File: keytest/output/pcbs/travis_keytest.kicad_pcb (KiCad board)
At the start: 2 copper layers, 51.4 x 51.4 mm, 4 parts

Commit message: key progress
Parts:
- LED1: value (none) -> SK6812mini-e
- S1: value (none) -> mx
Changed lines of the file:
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@@
   (page A3)
   (title_block
-    (title travis_key)
-    (rev 2024.03.20)
+    (title travis_keytest)
+    (rev 2024.03.21)
     (company "Travis Hardiman")
   )
@@
 (module MX (layer F.Cu)
     (at 100 100 45)
-    (fp_text reference "S1" (at 0 0) (layer F.SilkS)  (effects (font (size 1.27 1.27) (thickness 0.15))))
-    (fp_text value "" (at 0 0) (layer F.SilkS) hide (effects (font (size 1.27 1.27) (thickness 0.15))))
+    (fp_text reference "S1" (at 0 -3.25) (layer F.SilkS)  (effects (font (size 0.8 0.8) (thickness 0.15))))
+    (fp_text value "mx" (at 0 0) (layer F.SilkS) hide (effects (font (size 1 1) (thickness 0.15))))
     (fp_line (start -7 -6) (end -7 -7) (layer Dwgs.User) (width 0.15))
     (fp_line (start -7 7) (end -6 7) (layer Dwgs.User) (width 0.15))
@@
   (tags "Diode DO-35_SOD27 series Axial Horizontal pin pitch 7.62mm  length 4mm diameter 2mm")
   (at 100.0000 87.9438 315)
-  (fp_text reference "D1" (at 3.81 -2.12 315) (layer "B.SilkS")
+  (fp_text user "D1" (at 4 0 0) (layer "F.SilkS")
+    (effects (font (size 0.8 0.8) (thickness 0.15)))
+  )
+  (fp_text reference "D1" (at 5.985 1.921 315) (layer "B.SilkS")
     (effects (font (size 1 1) (thickness 0.15)) (justify mirror))
   )
-  (fp_text value "1N4148" (at 3.81 0 315) (layer "B.Fab")
-    (effects (font (size 0.8 1) (thickness 0.15)))
-  )
-  (fp_text user "K" (at 0 -1.8 315) (layer "B.SilkS")
-    (effects (font (size 1 1) (thickness 0.15)) (justify mirror))
-  )
-  (fp_text user "K" (at 0 -1.8 315) (layer "B.Fab")
-    (effects (font (size 1 1) (thickness 0.15)) (justify mirror))
+  (fp_text value "1N4148" (at 11.065 0 315) (layer "B.Fab")
+    (effects (font (size 0.8 0.8) (thickness 0.15)))
   )
   (fp_line (start 1.04 0) (end 1.69 0)
@@
   (at 103.5072 103.5072 45)
   (fp_text reference "LED1" (at -4.75 0 135) (layer B.SilkS)
-    (effects (font (size 1 1) (thickness 0.15)))
+    (effects (font (size 1 1) (thickness 0.15)) (justify mirror))
+  )
+  (fp_text value "SK6812mini-e" (at 0 -2.25 45) (layer "B.Fab")
+    (effects (font (size 0.5 0.5) (thickness 0.125)))
+  )
+  (fp_text user "LED_1" (at 2.70 -0.7 0) (layer "F.SilkS")
+    (effects (font (size 0.5 0.5) (thickness 0.125)))
   )
   (fp_line (start -1.6 -1.4) (end 1.6 -1.4) (layer Dwgs.User) (width 0.12))
@@
   (tags "C Disc series Radial pin pitch 5.00mm  diameter 4.7mm width 2.5mm Capacitor")
   (at 107.6368 104.1012 225)
-  (fp_text reference "C1" (at 2.5 -2.5 225) (layer B.SilkS)
-    (effects (font (size 1 1) (thickness 0.15)) (justify mirror))
+  (fp_text user "C1" (at 2.5 0 0) (layer F.SilkS)
+    (effects (font (size 0.8 0.8) (thickness 0.15)))
+  )
+  (fp_text reference "C1" (at -1.056 -0.082 225) (layer B.SilkS)
+    (effects (font (size 1 1) (thickness 0.15)) (justify right mirror))
   )
   (fp_text value "104" (at 2.5 2.5 225) (layer B.Fab)
-    (effects (font (size 1 1) (thickness 0.15)) (justify mirror))
+    (effects (font (size 1 1) (thickness 0.15)))
   )
   (fp_line (start 0.15 -1.25) (end 0.15 1.25) (layer B.Fab) (width 0.1))
@@
   (pad 1 thru_hole circle (at 0 0) (size 1.6 1.6) (drill 0.8) (layers *.Cu *.Mask) (net 6 "RAW"))
   (pad 2 thru_hole circle (at 5 0) (size 1.6 1.6) (drill 0.8) (layers *.Cu *.Mask) (net 7 "GND"))
-  (fp_text user %R (at 2.5 0) (layer B.Fab)
-    (effects (font (size 0.94 0.94) (thickness 0.141)))
+  (fp_text user %R (at 7.326 0) (layer B.Fab)
+    (effects (font (size 0.8 0.8) (thickness 0.141)) (justify ))
   )
   (model ${KISYS3DMOD}/Capacitor_THT.3dshapes/C_Disc_D4.7mm_W2.5mm_P5.00mm.wrl

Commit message: footprint wip
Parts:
- LED1: footprint ceoloide:led_SK6812mini-e (per-keysingle-side) -> ceoloide:led_SK6812mini-e (per-key single-side)
- S1: value mx -> Kailh MX Switch Sockets
- moved D1 8.47 mm to (107.8, 91.3), turned to 275 degrees
- moved C1 5.93 mm to (103.2, 108.1), turned to 185 degrees
- moved LED1 3.39 mm to (100.4, 104.9), turned to 5 degrees
- turned S1 to 5 degrees
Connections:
- LED1 pad 2: LED_1 -> LED_0
- LED1 pad 4: LED_0 -> LED_1
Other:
- board size 51.4 x 51.4 mm -> 40.8 x 40.8 mm
- board text added: "C1"
- board text added: "D1"
- board text added: "LED_1"

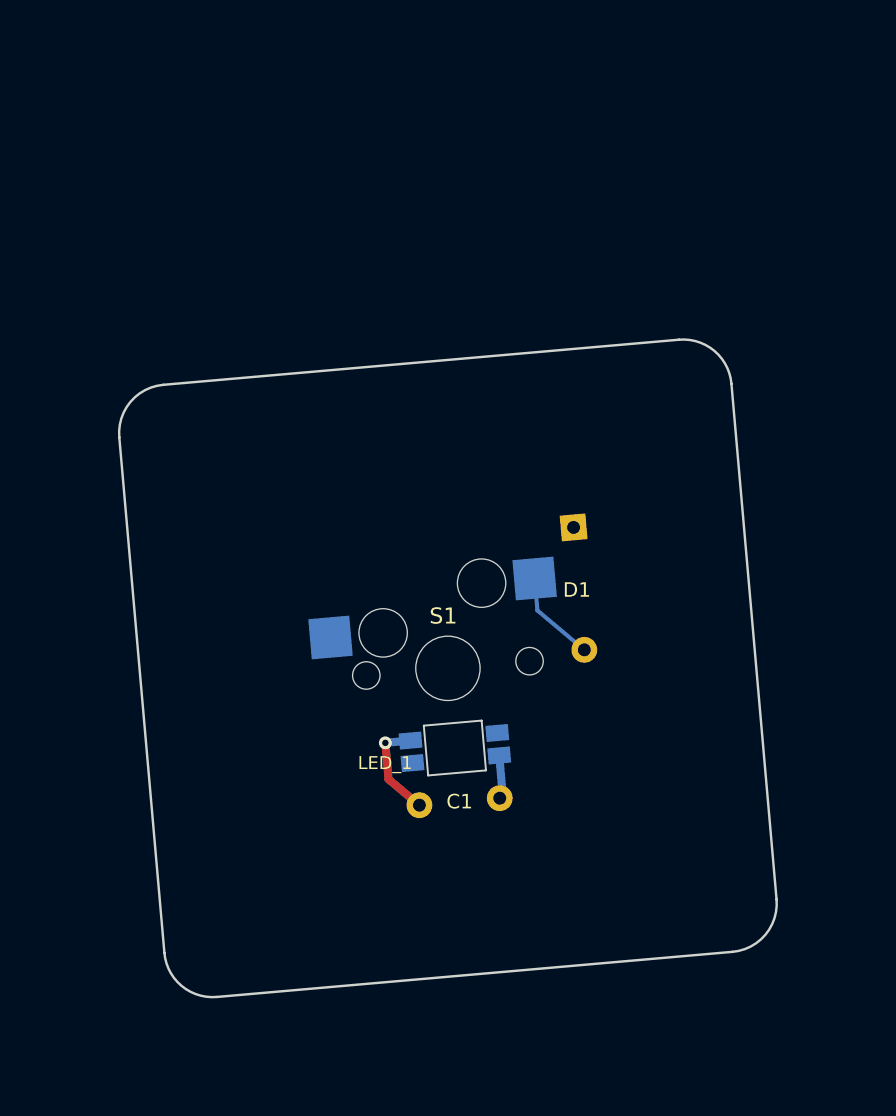
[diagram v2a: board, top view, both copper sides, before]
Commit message: rtl option added
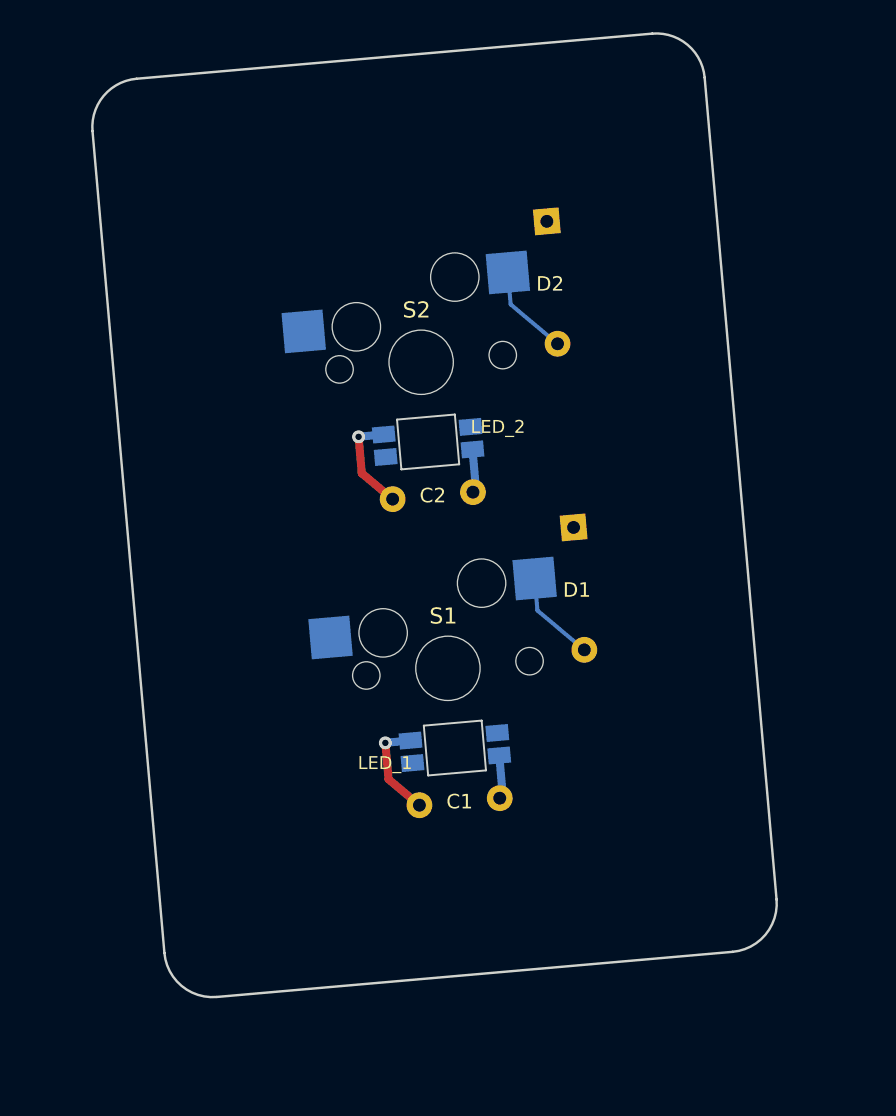
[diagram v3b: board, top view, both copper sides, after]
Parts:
- added C2: 104, C_Disc_D4.7mm_W2.5mm_P5.00mm, B.Cu at (96.6, 89.5)
- added D2: 1N4148, Diode_DO-35, B.Cu at (106.1, 72.3)
- added LED2: SK6812mini-e, ceoloide:led_SK6812mini-e (per-key single-side), B.Cu at (98.8, 86.0)
- added S2: Kailh MX Switch Sockets, MX, F.Cu at (98.3, 81.0)
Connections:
- LED1 pad 2: LED_0 -> LED_2
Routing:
- net RAW: track 2.72 -> 9.06 mm, vias 0 -> 1
- net single_A_two: track 0.00 -> 5.79 mm
- net GND: track 6.34 -> 9.06 mm
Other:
- board size 40.8 x 40.8 mm -> 42.4 x 59.7 mm
- board text added: "C2"
- board text added: "D2"
- board text added: "LED_2"
